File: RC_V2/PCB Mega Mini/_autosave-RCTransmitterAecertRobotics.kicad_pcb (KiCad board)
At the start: 2 copper layers, 124.5 x 86.4 mm, 40 parts, among them K1 KCD1 Power Switch

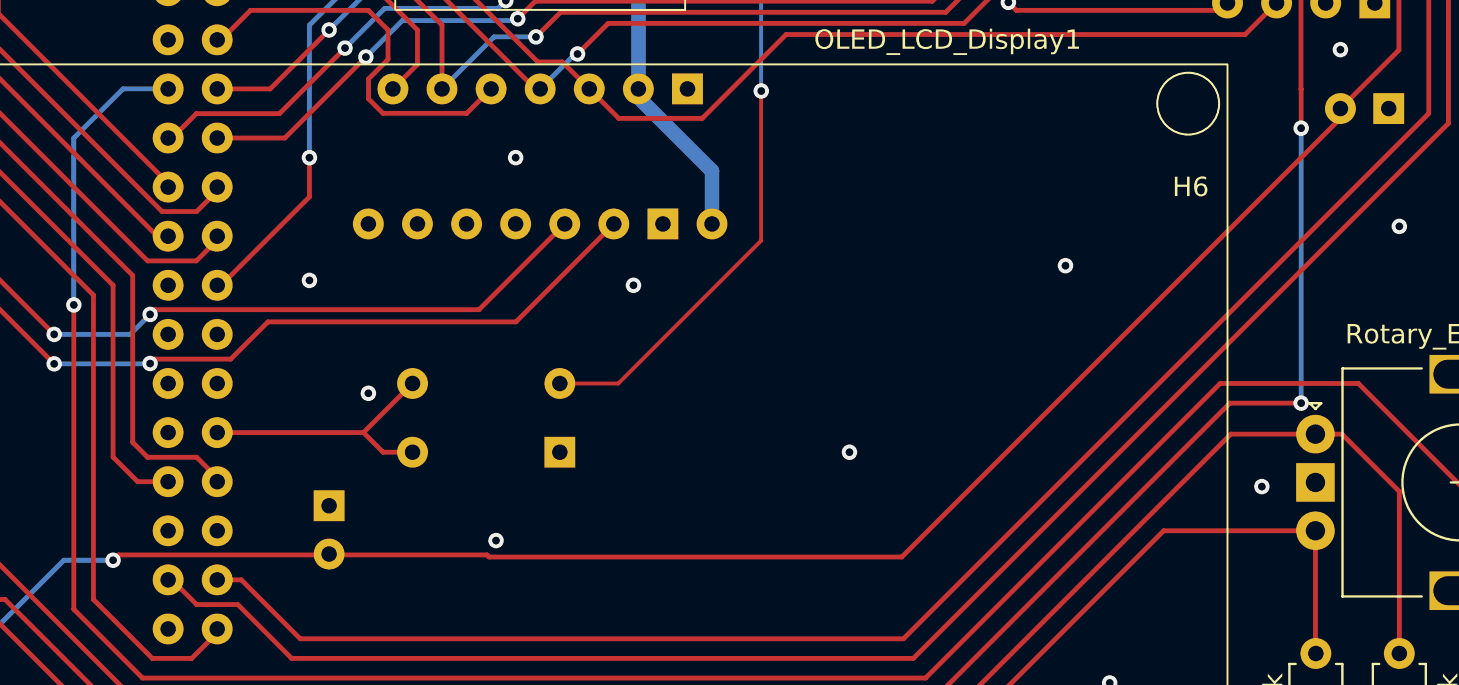
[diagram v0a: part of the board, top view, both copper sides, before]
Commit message: updated rc code to work with new controller
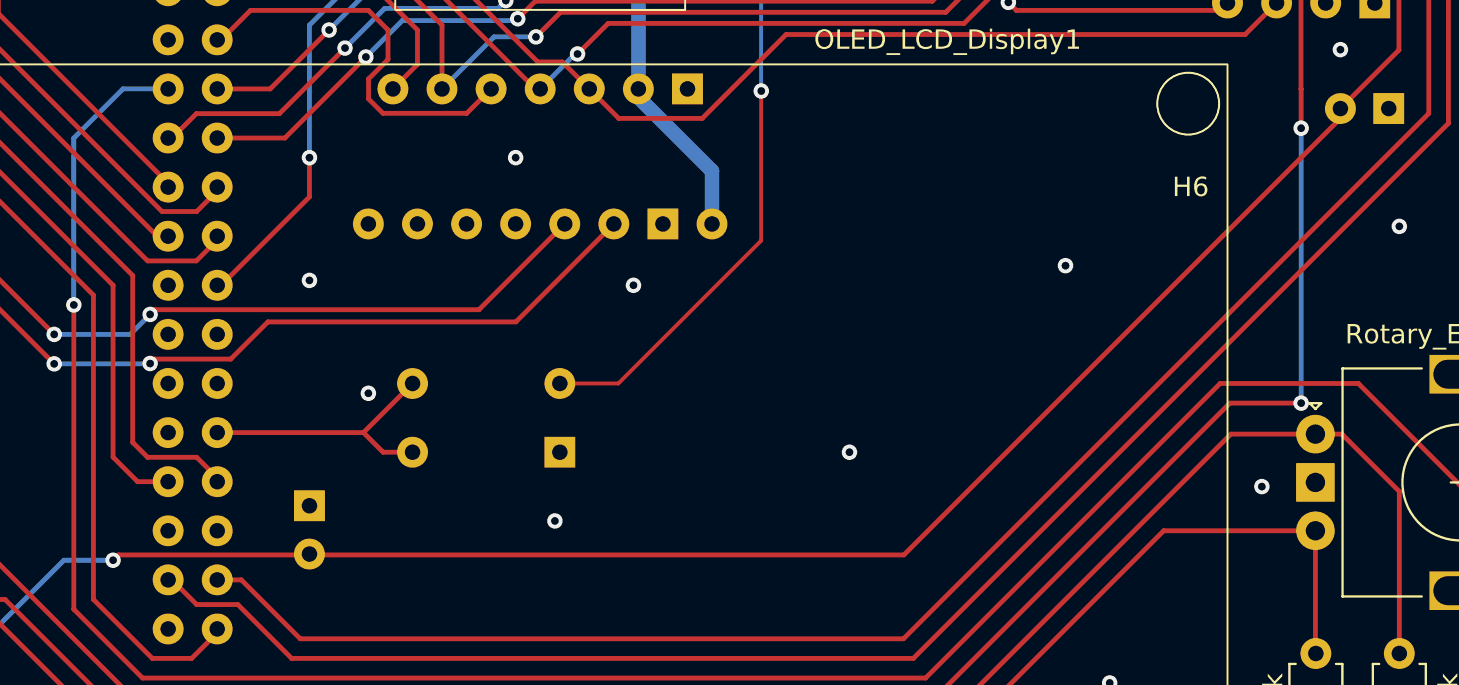
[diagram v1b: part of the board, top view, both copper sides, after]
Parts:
- moved C2 1.02 mm to (129.0, 123.1)
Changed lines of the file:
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@@
   )
   (footprint "Capacitor_THT:CP_Radial_D5.0mm_P2.50mm" (layer "B.Cu")
-    (at 130.048 123.125113 90)
+    (at 129.032 123.125113 90)
     (descr "CP, Radial series, Radial, pin pitch=2.50mm, , diameter=5mm, Electrolytic Capacitor")
     (tags "CP Radial series Radial pin pitch 2.50mm  diameter 5mm Electrolytic Capacitor")
@@
   (via (at 102.108 98.044) (size 0.8) (drill 0.4) (layers "F.Cu" "B.Cu") (free) (net 2))
   (via (at 168.148 108.204) (size 0.8) (drill 0.4) (layers "F.Cu" "B.Cu") (free) (net 2))
-  (via (at 138.684 122.428) (size 0.8) (drill 0.4) (layers "F.Cu" "B.Cu") (free) (net 2))
+  (via (at 141.732 121.412) (size 0.8) (drill 0.4) (layers "F.Cu" "B.Cu") (free) (net 2))
   (via (at 93.472 99.568) (size 0.8) (drill 0.4) (layers "F.Cu" "B.Cu") (free) (net 2))
   (via (at 161.036 73.66) (size 0.8) (drill 0.4) (layers "F.Cu" "B.Cu") (free) (net 2))
@@
   (via (at 185.42 106.172) (size 0.8) (drill 0.4) (layers "F.Cu" "B.Cu") (free) (net 2))
   (via (at 187.452 75.184) (size 0.8) (drill 0.4) (layers "F.Cu" "B.Cu") (free) (net 2))
+  (segment (start 119.146 123.17) (end 118.872 123.444) (width 0.25) (layer "F.Cu") (net 3))
   (segment (start 106.819 129.964) (end 109.4535 127.3295) (width 0.25) (layer "F.Cu") (net 3))
   (segment (start 88.265 132.08) (end 90.805 132.08) (width 0.25) (layer "F.Cu") (net 3))
-  (segment (start 182.372 100.584) (end 159.678 123.278) (width 0.25) (layer "F.Cu") (net 3))
-  (segment (start 119.146 123.17) (end 118.872 123.444) (width 0.25) (layer "F.Cu") (net 3))
   (segment (start 182.372 100.076) (end 182.372 100.584) (width 0.25) (layer "F.Cu") (net 3))
-  (segment (start 159.678 123.278) (end 138.331918 123.278) (width 0.25) (layer "F.Cu") (net 3))
   (segment (start 185.4 93.325) (end 185.4 97.048) (width 0.25) (layer "F.Cu") (net 3))
   (segment (start 97.973 129.964) (end 106.819 129.964) (width 0.25) (layer "F.Cu") (net 3))
   (segment (start 97.889 130.048) (end 97.973 129.964) (width 0.25) (layer "F.Cu") (net 3))
+  (segment (start 182.372 100.584) (end 159.786 123.17) (width 0.25) (layer "F.Cu") (net 3))
   (segment (start 185.4 97.048) (end 182.372 100.076) (width 0.25) (layer "F.Cu") (net 3))
-  (segment (start 138.223918 123.17) (end 119.146 123.17) (width 0.25) (layer "F.Cu") (net 3))
   (segment (start 184.15 92.075) (end 185.4 93.325) (width 0.25) (layer "F.Cu") (net 3))
-  (segment (start 138.331918 123.278) (end 138.223918 123.17) (width 0.25) (layer "F.Cu") (net 3))
+  (segment (start 159.786 123.17) (end 119.146 123.17) (width 0.25) (layer "F.Cu") (net 3))
   (segment (start 109.4535 127.3295) (end 112.268 127.3295) (width 0.25) (layer "F.Cu") (net 3))
   (via (at 112.268 127.3295) (size 0.8) (drill 0.4) (layers "F.Cu" "B.Cu") (net 3))
